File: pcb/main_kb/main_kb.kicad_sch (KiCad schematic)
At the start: 23 parts, among them J1 AVR-ISP-6, J2 USB_C_Receptacle_USB2.0, U1 ATMEGA32U4-AU

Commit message: Fixed SDA/SCL Step-up Resistors
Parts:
- removed 5.1k: R, symbol Device:R
- added R5, R6: 4.7k, symbol Device:R
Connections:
- net +5V: now also U1.34 (VCC), U1.44 (AVCC), U2.1 (VCC), R5.2, R6.2
- net GND: now also U1.23 (GND), U1.35 (GND), U1.43 (GND)
- net SCL: now also R5.1
- net SDA: now also R6.1
- no-connect marks 13 -> 8
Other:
- moved on the sheet: J2, R2, R3, R4, R7, R8, S1, U2

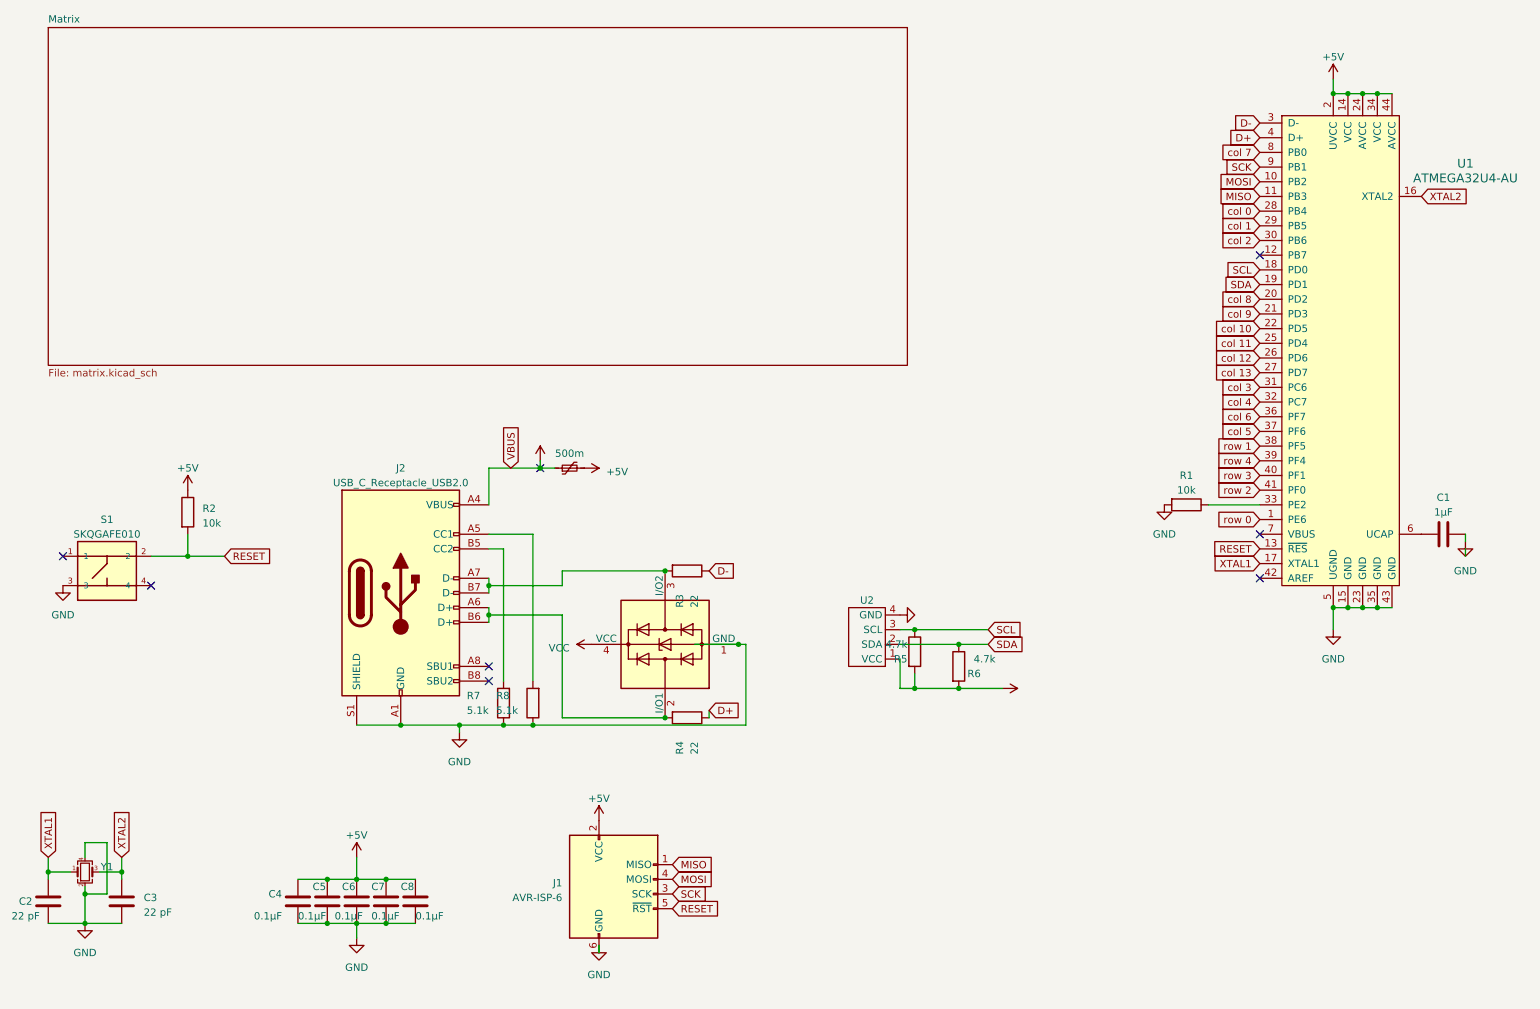
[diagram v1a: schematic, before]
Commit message: Changed layout, added layout diagram
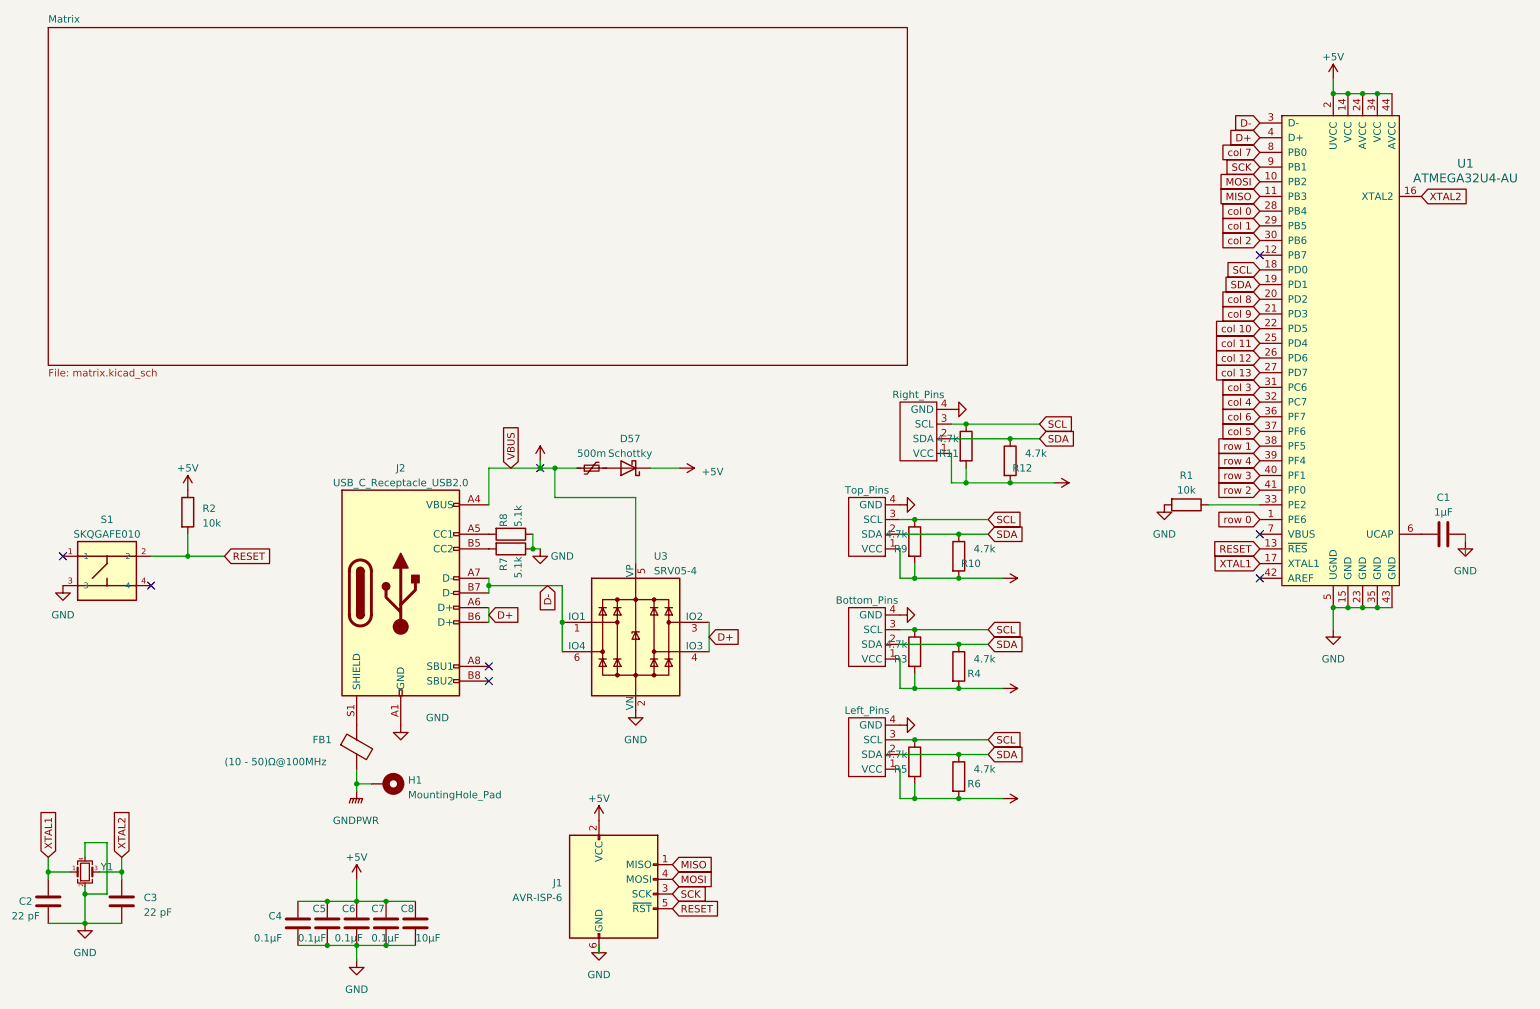
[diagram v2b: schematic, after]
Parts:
- removed D1: PRTR5V0U2X, Package_TO_SOT_SMD:SOT-143, symbol Power_Protection:PRTR5V0U2X
- added Bottom_Pins, Right_Pins, Top_Pins: ~, symbol local:HTP-CON-M411PR-M
- added D57: Schottky, symbol Device:D_Schottky
- added FB1: (10 - 50)Ω@100MHz, symbol Device:FerriteBead
- added H1: MountingHole_Pad, symbol Mechanical:MountingHole_Pad
- added R10, R11, R12, R9: 4.7k, symbol Device:R
- added U3: SRV05-4, PCM_marbastlib-various:SOT-23-6-routable, symbol marbastlib-various:SRV05-4
- C8: value 0.1µF -> 10µF
- R3, R4: value 22 -> 4.7k
- renumbered U2 to Left_Pins
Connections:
- net +5V: now also R3.2, R4.2, Bottom_Pins.1 (VCC), D57.1 (K), R10.2, R11.2, R12.2, R9.2, Right_Pins.1 (VCC), Top_Pins.1 (VCC); no longer F1.2
- net D+: now also J2.A6 (D+), J2.B6 (D+), U3.3 (IO2), U3.4 (IO3); no longer R4.1
- net D-: now also J2.A7 (D-), J2.B7 (D-), U3.1 (IO1), U3.6 (IO4); no longer R3.1
- net GND: now also Bottom_Pins.4 (GND), Right_Pins.4 (GND), Top_Pins.4 (GND), U3.2 (VN); no longer J2.S1 (SHIELD)
- net SCL: now also R3.1, Bottom_Pins.3 (SCL), R11.1, R9.1, Right_Pins.3 (SCL), Top_Pins.3 (SCL)
- net SDA: now also R4.1, Bottom_Pins.2 (SDA), R10.1, R12.1, Right_Pins.2 (SDA), Top_Pins.2 (SDA)
- net VCC: now also U3.5 (VP)
- new net: D57.2 (A), F1.2
- new net: FB1.1, J2.S1 (SHIELD)
- new net GNDPWR: FB1.2, H1.1
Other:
- title: (none) ->  Keyflex QWERTY [P.O.D] (C) Rithul K
- moved on the sheet: C4, C5, C6, C7, C8, Left_Pins, R5, R6, R7, R8
